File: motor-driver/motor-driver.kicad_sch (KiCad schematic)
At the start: 6 parts, among them Q1 NMOS, Q2 NMOS, Q3 NMOS, Q4 NMOS, Q5 NMOS, Q6 NMOS

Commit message: Testing commit
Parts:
- removed Q2, Q3, Q5, Q6: NMOS, symbol Simulation_SPICE:NMOS
- added C1: 100uF, symbol Device:C
- added C2, C6: 0.1uF, symbol Device:C
- added C3: 0.1uF, Capacitor_SMD:C_0603_1608Metric, symbol Device:C
- added C4: 1uF, Capacitor_SMD:C_0603_1608Metric, symbol Device:C
- added C5: 1uF, symbol Device:C
- added C7, C8: 100pF, symbol Device:C
- added C9: 10uF, Capacitor_SMD:C_0603_1608Metric, symbol Device:C
- added D1: 1N5401, Diode_THT:D_DO-201AD_P15.24mm_Horizontal, symbol Diode:1N5401
- added R1, R3, R4, R5: 0, symbol Device:R
- added R2: 10, symbol Device:R
- added U1: ESP32-C6, ESP32-C6:QFN40P500X500X90-41N, symbol ESP32-C6:ESP32-C6
- added U3: FAN7388, Package_SO:SOIC-20W_7.5x12.8mm_P1.27mm, symbol Driver_FET:FAN7388
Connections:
- net GND: now also C1.2, C3.2, C4.2, C5.2, C6.2, C7.1, C8.1, C9.2, R2.1, U3.11 (GND)
- net +14V: now reaches Q1.1 (D)
- net +14V: now also C1.1, C5.1, C6.1, D1.2 (A), U3.12 (VDD)
- net at Q1.2 (G): now also R1.2
- net at Q1.3 (S): now also Q4.1 (D), C2.1, U3.18 (VS1)
- net at Q4.2 (G): now also R3.2
- net at Q4.3 (S): now also R2.2
- new net: C7.2, R5.2, U3.2 (LIN1)
- new net: C8.2, R4.2, U3.1 (HIN1)
- new net: R3.1, U3.17 (LO1)
- new net: R1.1, U3.19 (HO1)
- new net: C2.2, D1.1 (K), U3.20 (VB1)
- new net +5V: C3.1, C4.1, C9.1
- new net PWM_U_H: R4.1
- new net PWM_U_L: R5.1
- new net VDDA3P3: U1.2 (VDDA3P3), U1.3 (VDDA3P3)
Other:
- moved on the sheet: Q1, Q4

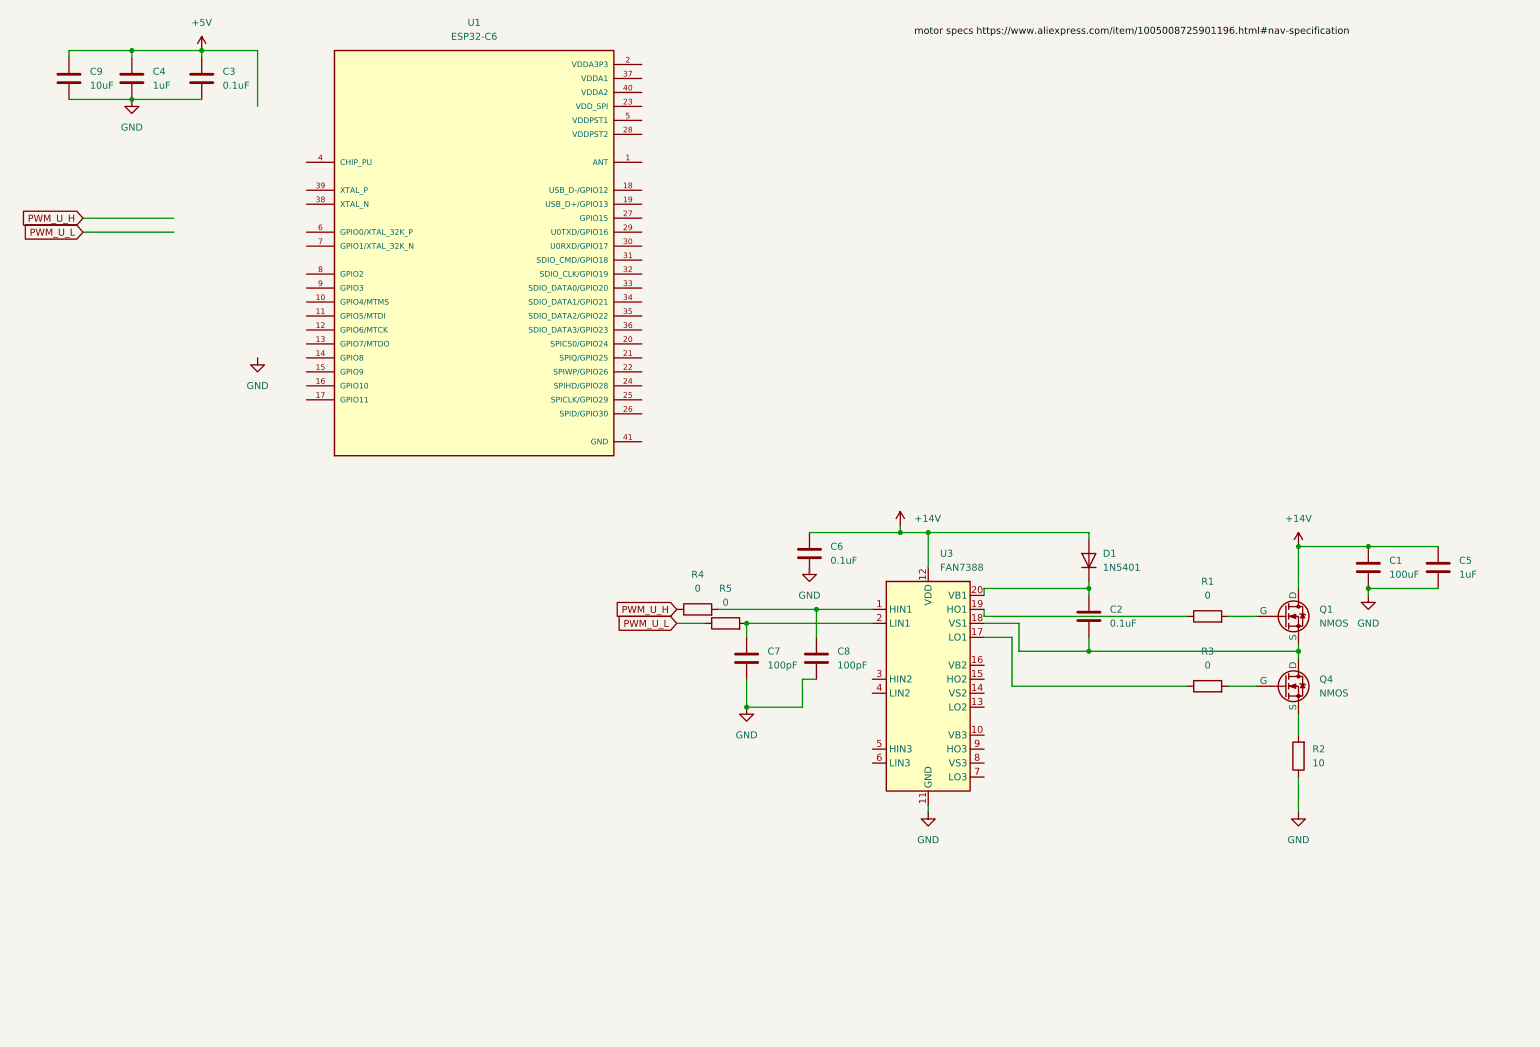
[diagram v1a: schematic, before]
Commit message: motor driver schematic updated
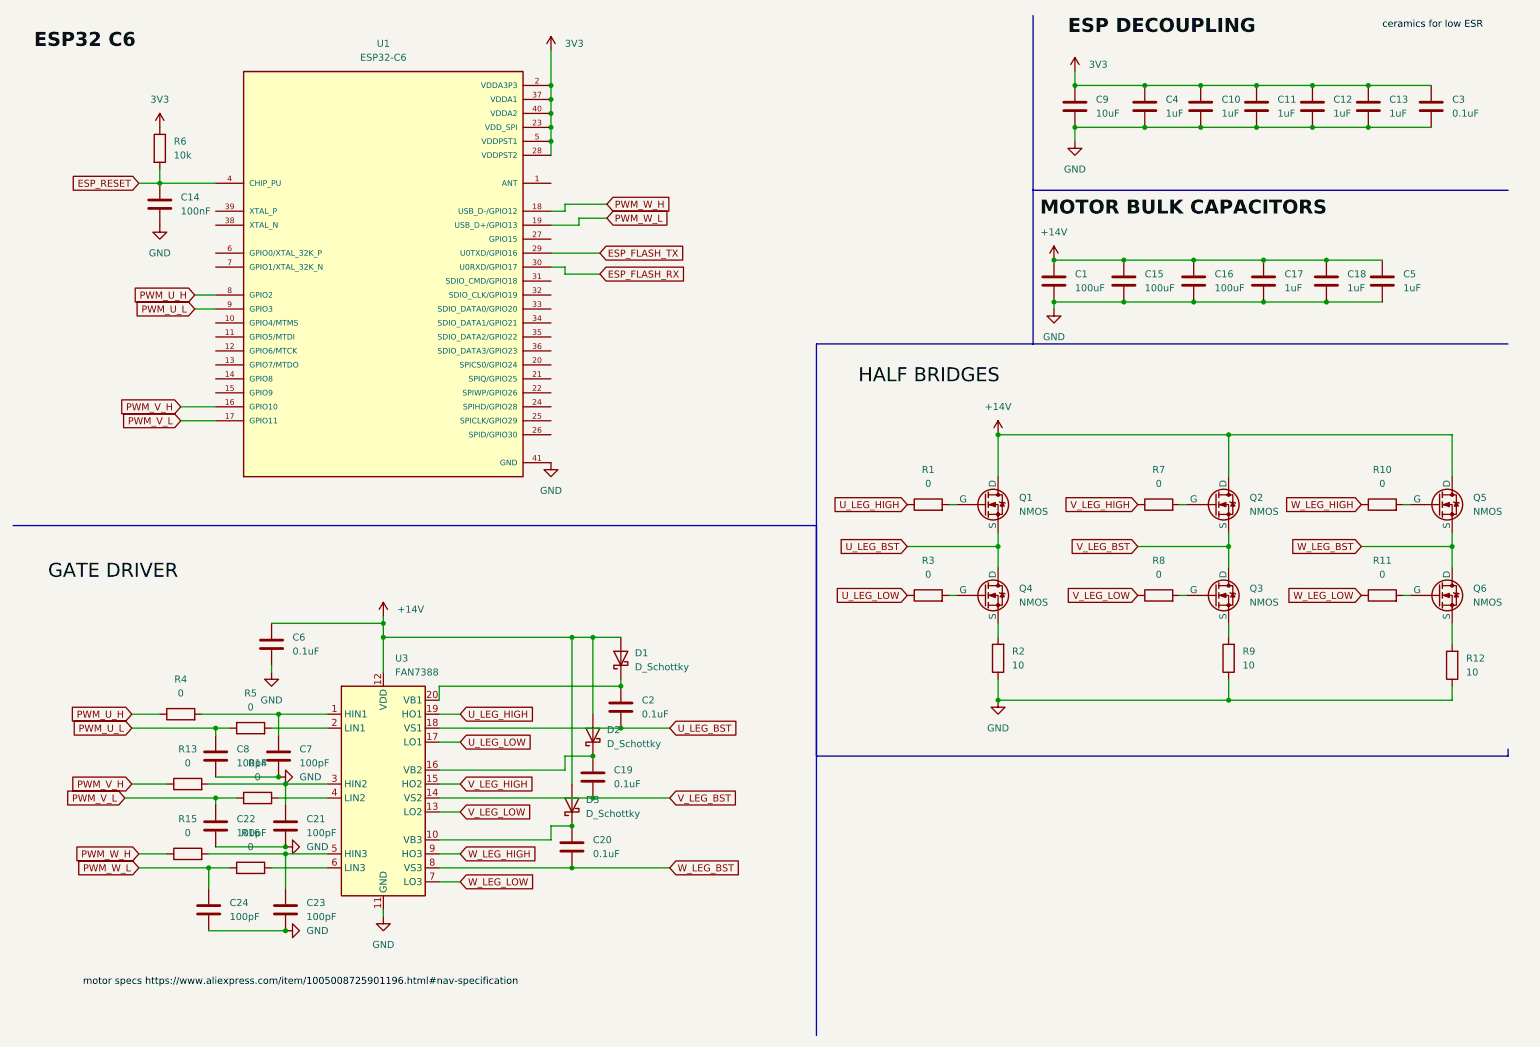
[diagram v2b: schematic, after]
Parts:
- removed D1: 1N5401, Diode_THT:D_DO-201AD_P15.24mm_Horizontal, symbol Diode:1N5401
- added C10, C11, C12, C13: 1uF, Capacitor_SMD:C_0603_1608Metric, symbol Device:C
- added C14: 100nF, symbol Device:C
- added C15, C16: 100uF, Capacitor_SMD:C_0201_0603Metric_Pad0.64x0.40mm_HandSolder, symbol Device:C
- added C17, C18: 1uF, Capacitor_SMD:C_0201_0603Metric_Pad0.64x0.40mm_HandSolder, symbol Device:C
- added C19, C20: 0.1uF, Capacitor_SMD:C_0201_0603Metric_Pad0.64x0.40mm_HandSolder, symbol Device:C
- added C21, C22, C23, C24: 100pF, symbol Device:C
- added D1, D2, D3: D_Schottky, Diode_SMD:D_0201_0603Metric_Pad0.64x0.40mm_HandSolder, symbol Device:D_Schottky
- added Q2, Q3, Q5, Q6: NMOS, symbol Simulation_SPICE:NMOS
- added R10, R11, R13, R14, R15, R16, R7, R8: 0, symbol Device:R
- added R12, R9: 10, symbol Device:R
- added R6: 10k, symbol Device:R
- C1, C2, C5: footprint (none) -> Capacitor_SMD:C_0201_0603Metric_Pad0.64x0.40mm_HandSolder
- C6: footprint (none) -> Capacitor_SMD:C_0603_1608Metric_Pad1.08x0.95mm_HandSolder
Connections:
- net +5V is gone; now on net 3V3: C3.1, C4.1, C9.1
- net VDDA3P3 is gone; now on net 3V3: U1.2 (VDDA3P3), U1.3 (VDDA3P3)
- net +14V: now also C15.1, C16.1, C17.1, C18.1, D1.2 (A), D2.2 (A), D3.2 (A), Q2.1 (D), Q5.1 (D)
- net GND: now also C7.2, C8.2, U1.41 (GND), C10.2, C11.2, C12.2, C13.2, C14.2, C15.2, C16.2, C17.2, C18.2, C21.2, C22.2, C23.2, C24.2, R12.1, R9.1; no longer C7.1, C8.1
- net PWM_U_H: now also U1.8 (GPIO2)
- net PWM_U_L: now also C8.1, U1.9 (GPIO3)
- net at R5.2, U3.2 (LIN1): no longer C7.2
- net at R4.2, U3.1 (HIN1): now also C7.1; no longer C8.2
- net U_LEG_BST: now reaches C2.1, Q1.3 (S), Q4.1 (D), U3.18 (VS1)
- net at U3.10 (VB3): now also C20.2, D3.1 (K)
- net V_LEG_LOW: now reaches U3.13 (LO2)
- net V_LEG_LOW: now also R8.1
- net V_LEG_BST: now reaches U3.14 (VS2)
- net V_LEG_BST: now also C19.1, Q2.3 (S), Q3.1 (D)
- net V_LEG_HIGH: now reaches U3.15 (HO2)
- net V_LEG_HIGH: now also R7.1
- net at U3.16 (VB2): now also C19.2, D2.1 (K)
- net U_LEG_LOW: now reaches R3.1, U3.17 (LO1)
- net U_LEG_HIGH: now reaches R1.1, U3.19 (HO1)
- net at C2.2, U3.20 (VB1): now also D1.1 (K)
- net at U3.3 (HIN2): now also C21.1, R13.2
- net at U3.4 (LIN2): now also R14.2
- net at U3.5 (HIN3): now also C23.1, R15.2
- net at U3.6 (LIN3): now also R16.2
- net W_LEG_LOW: now reaches U3.7 (LO3)
- net W_LEG_LOW: now also R11.1
- net W_LEG_BST: now reaches U3.8 (VS3)
- net W_LEG_BST: now also C20.1, Q5.3 (S), Q6.1 (D)
- net W_LEG_HIGH: now reaches U3.9 (HO3)
- net W_LEG_HIGH: now also R10.1
- net PWM_V_H: now reaches U1.16 (GPIO10)
- net PWM_V_H: now also R13.1
- net PWM_V_L: now reaches U1.17 (GPIO11)
- net PWM_V_L: now also C22.1, R14.1
- net PWM_W_H: now reaches U1.18 (USB_D-/GPIO12)
- net PWM_W_H: now also R15.1
- net PWM_W_L: now reaches U1.19 (USB_D+/GPIO13)
- net PWM_W_L: now also C24.1, R16.1
- net 3V3: now reaches U1.23 (VDD_SPI)
- net 3V3: now also U1.28 (VDDPST2), U1.37 (VDDA1), U1.40 (VDDA2), U1.5 (VDDPST1), C10.1, C11.1, C12.1, C13.1, R6.1
- net ESP_FLASH_TX: now reaches U1.29 (U0TXD/GPIO16)
- net ESP_FLASH_RX: now reaches U1.30 (U0RXD/GPIO17)
- net ESP_RESET: now reaches U1.4 (CHIP_PU)
- net ESP_RESET: now also C14.1, R6.2
- new net: Q2.2 (G), R7.2
- new net: Q3.3 (S), R9.2
- new net: Q3.2 (G), R8.2
- new net: Q6.2 (G), R11.2
- new net: Q5.2 (G), R10.2
- new net: Q6.3 (S), R12.2
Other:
- moved on the sheet: C1, C2, C3, C4, C5, C6, C9, Q1, Q4, R1, R2, R3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

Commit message: modified bulk capacitor setup
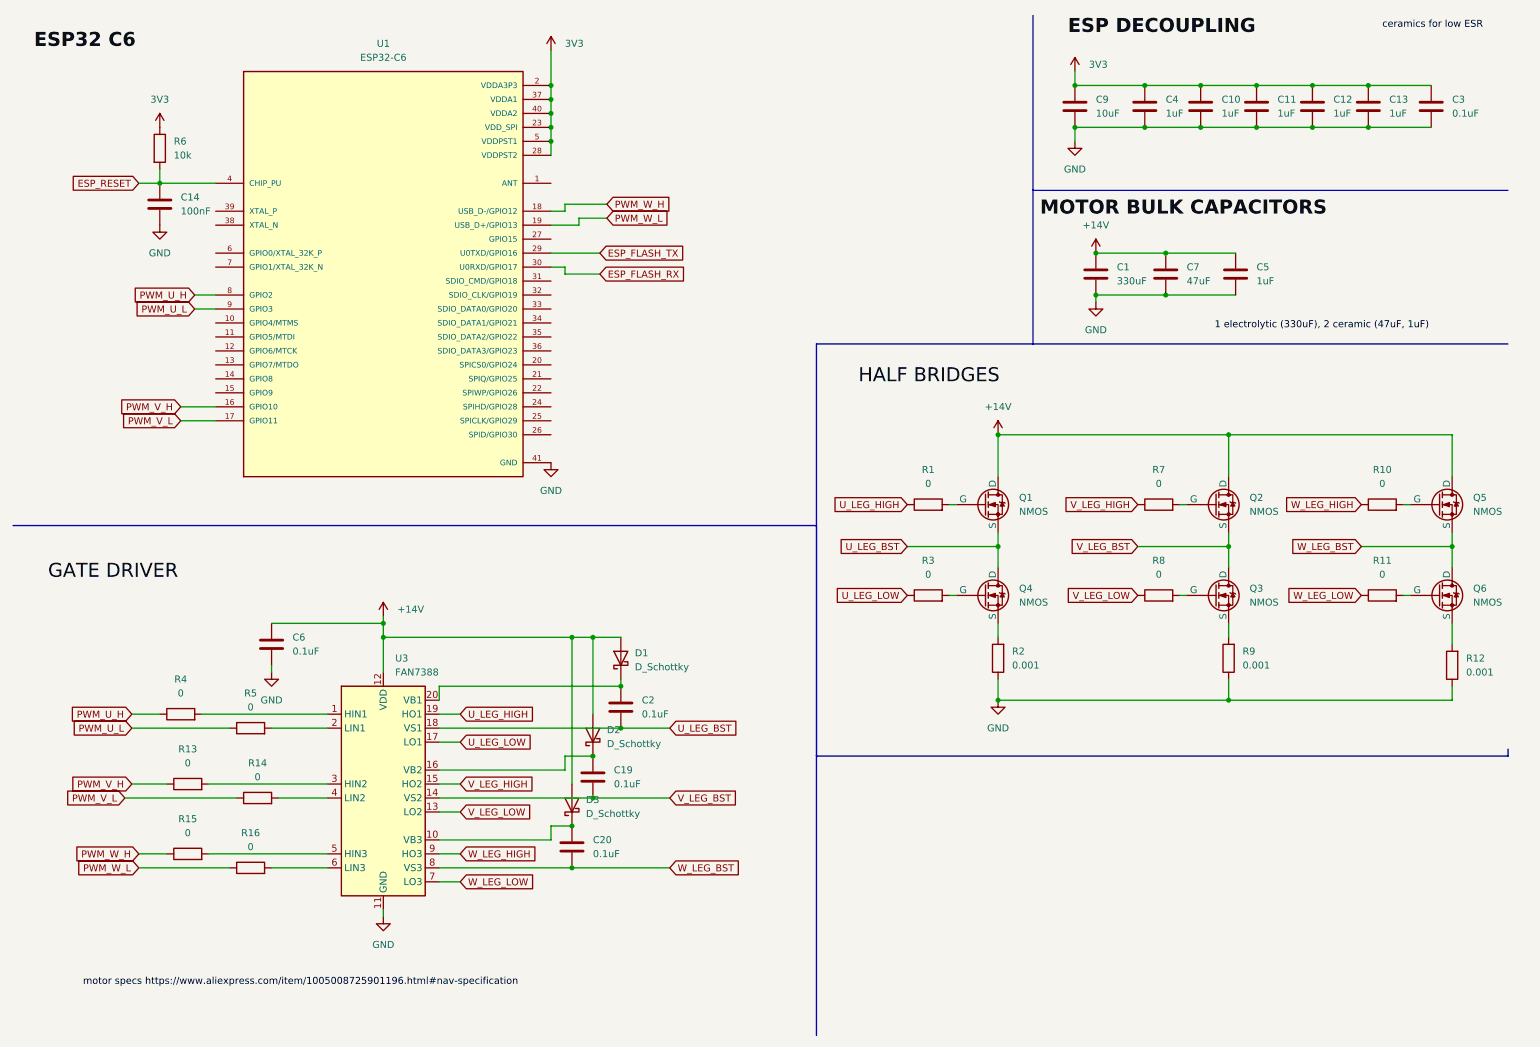
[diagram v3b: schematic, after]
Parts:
- removed C15, C16: 100uF, Capacitor_SMD:C_0201_0603Metric_Pad0.64x0.40mm_HandSolder, symbol Device:C
- removed C17, C18: 1uF, Capacitor_SMD:C_0201_0603Metric_Pad0.64x0.40mm_HandSolder, symbol Device:C
- removed C21, C22, C23, C24, C8: 100pF, symbol Device:C
- C1: value 100uF -> 330uF
- C7: value 100pF -> 47uF; footprint (none) -> Capacitor_SMD:C_0201_0603Metric_Pad0.64x0.40mm_HandSolder
- R12, R2, R9: value 10 -> 0.001
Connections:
- net +14V: now also C7.1
- net at R4.2, U3.1 (HIN1): no longer C7.1
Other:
- moved on the sheet: C1, C5

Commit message: current sense finshed for motor driver
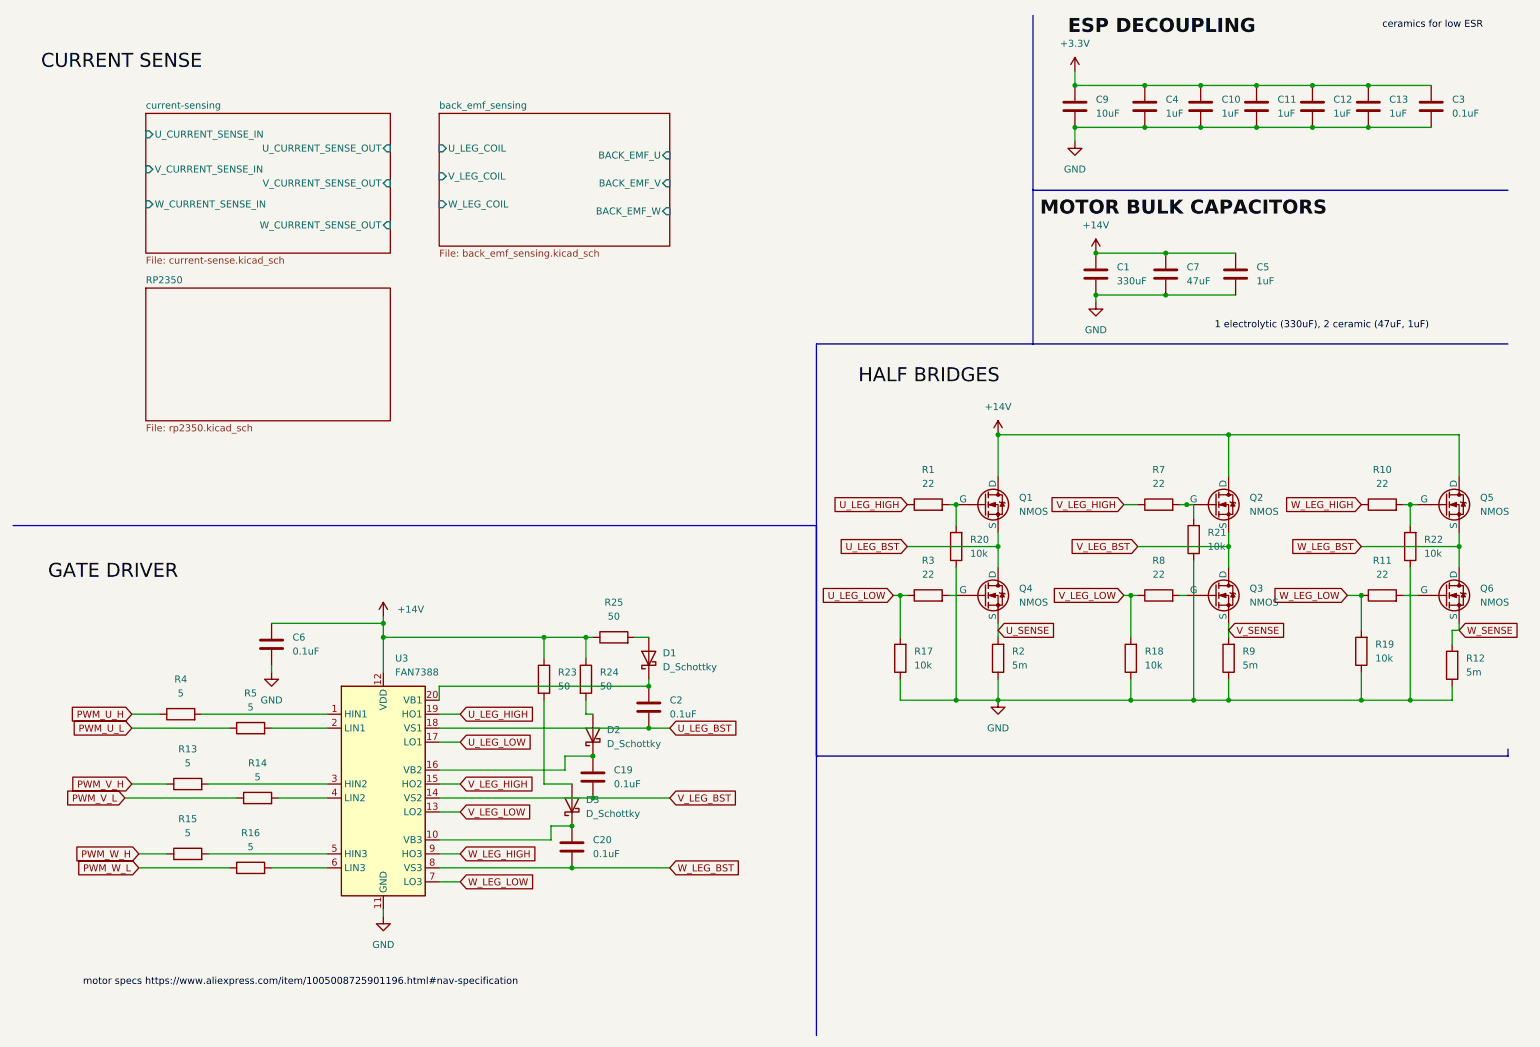
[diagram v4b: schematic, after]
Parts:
- removed C14: 100nF, symbol Device:C
- removed R6: 10k, symbol Device:R
- removed U1: ESP32-C6, ESP32-C6:QFN40P500X500X90-41N, symbol ESP32-C6:ESP32-C6
- added R17, R18, R19, R20, R21, R22: 10k, symbol Device:R
- added R23, R24, R25: 50, symbol Device:R
- R1, R10, R11, R3, R7, R8: value 0 -> 22
- R12, R2, R9: value 0.001 -> 5m
- R13, R14, R15, R16, R4, R5: value 0 -> 5
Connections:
- net +14V: now also R23.1, R24.1, R25.1; no longer D1.2 (A), D2.2 (A), D3.2 (A)
- net GND: now also R17.1, R18.1, R19.1, R20.1, R21.1, R22.1
- net U_LEG_LOW: now also R17.2
- net V_LEG_LOW: now also R18.2
- net W_LEG_LOW: now also R19.2
- net at Q2.2 (G), R7.2: now also R21.2
- net V_SENSE: now reaches Q3.3 (S), R9.2
- net at Q1.2 (G), R1.2: now also R20.2
- net at Q5.2 (G), R10.2: now also R22.2
- net U_SENSE: now reaches Q4.3 (S), R2.2
- net W_SENSE: now reaches Q6.3 (S), R12.2
- net 3V3 renamed +3.3V
- new net: D2.2 (A), R24.2
- new net: D3.2 (A), R23.2
- new net: D1.2 (A), R25.2
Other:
- added sheet RP2350 (rp2350.kicad_sch)
- added sheet back_emf_sensing (back_emf_sensing.kicad_sch)
- added sheet current-sensing (current-sense.kicad_sch)
- moved on the sheet: C2, D1, Q5, Q6
